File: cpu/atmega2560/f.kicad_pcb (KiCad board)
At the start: 2 copper layers, 76.8 x 81.3 mm, 31 parts, among them J1 bus, J10 RS485_0, J11 RS485_1, J14 RTC_DS3231, J2 ICSP, J3 fm_cpu_i, J4 dio_channel_i, SW1 default, SW2 reset, U1 ATmega2560-16AU, U4 MC34064D, Y1 16M

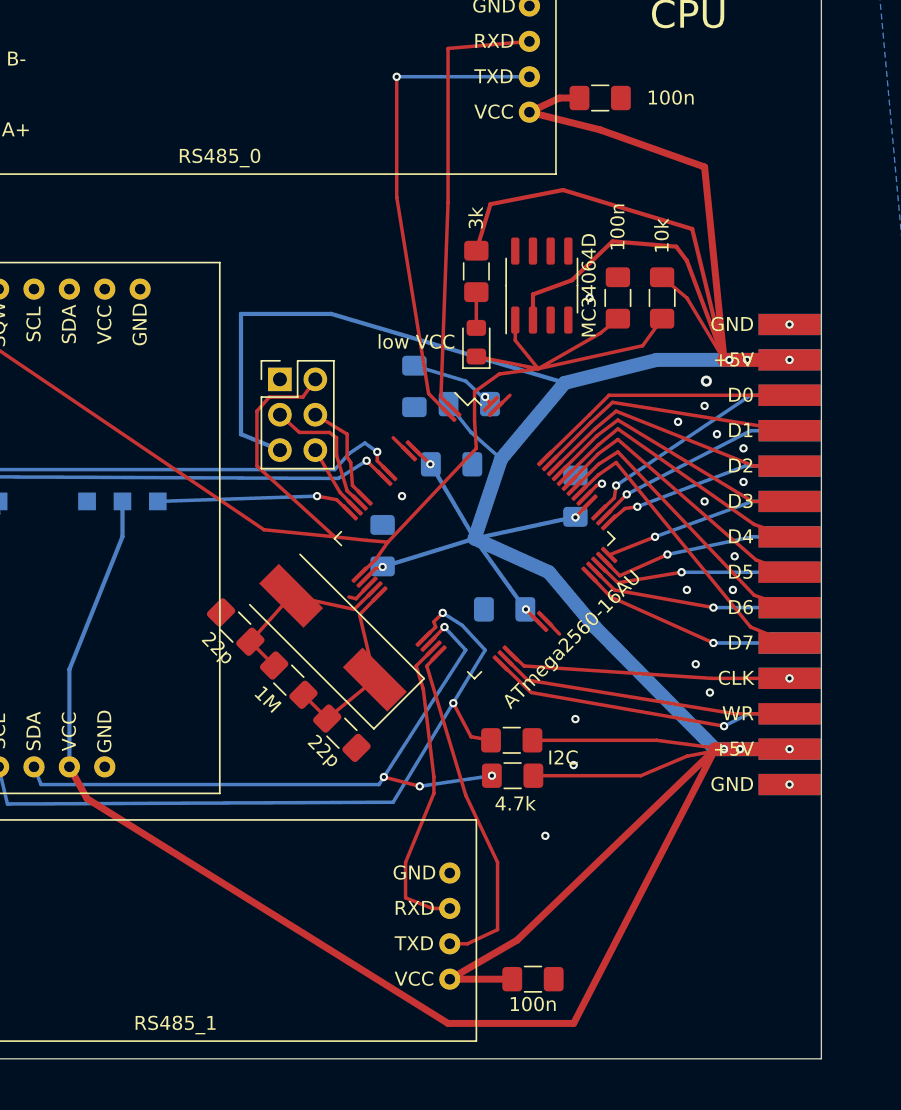
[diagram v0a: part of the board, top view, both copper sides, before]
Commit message: voltage regulator for each module
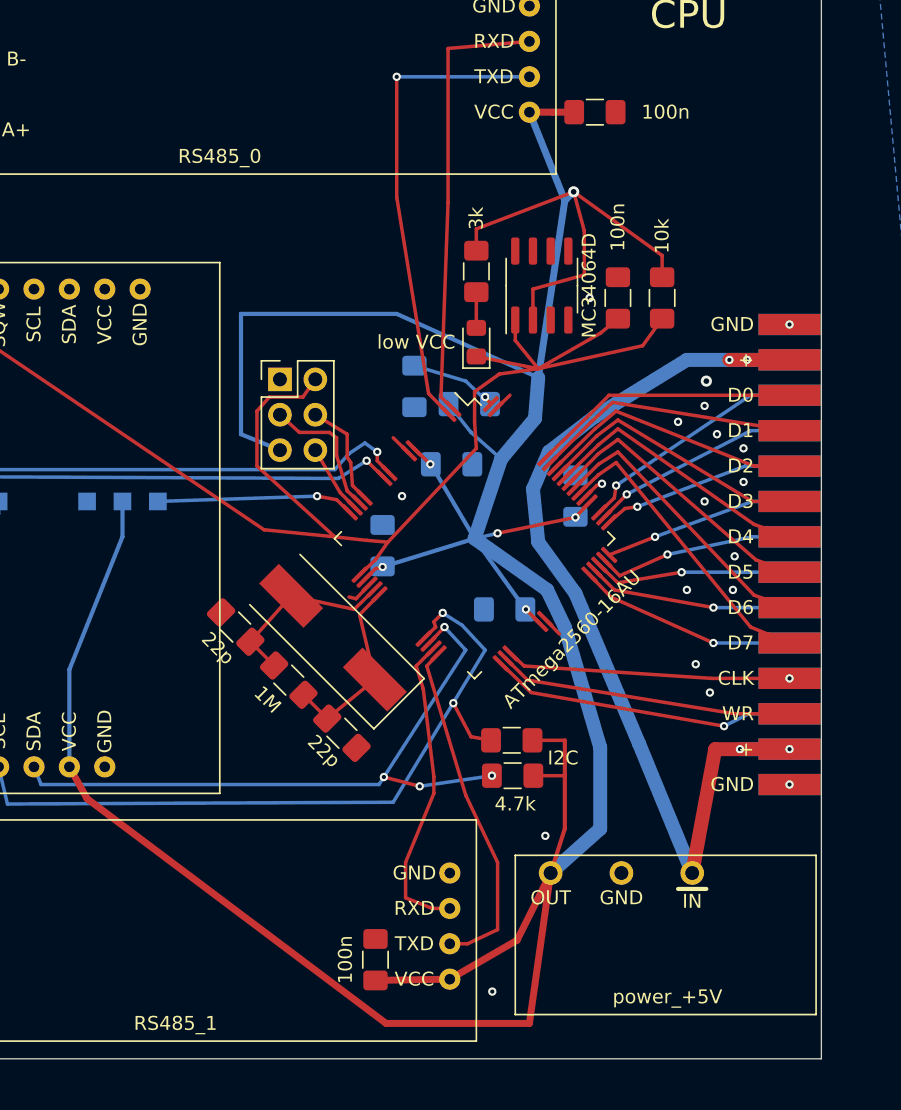
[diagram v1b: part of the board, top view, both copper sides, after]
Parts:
- added J5: power_+5V, plc88:power_i, F.Cu at (105.7, 140.3)
- J4: value dio_channel_i -> digital_output
- moved C7 11.4 mm to (76.6, 136.4), turned to 90 degrees
- moved C8 1.09 mm to (92.3, 75.6)
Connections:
- J1 pad 25: +5V -> VP
- J1 pad 26: +5V -> VP
- J1 pad 3: +5V -> VP
- J1 pad 4: +5V -> VP
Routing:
- net +5V: track 372.8 -> 269.4 mm, vias 10 -> 6
- net VP: track 0.00 -> 74.6 mm, vias 0 -> 4
- net GND: vias 21 -> 20
